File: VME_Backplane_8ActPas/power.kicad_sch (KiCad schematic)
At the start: 7 parts, among them U1 TCA0372, U2 TCA0372, X1 Conn_01x05

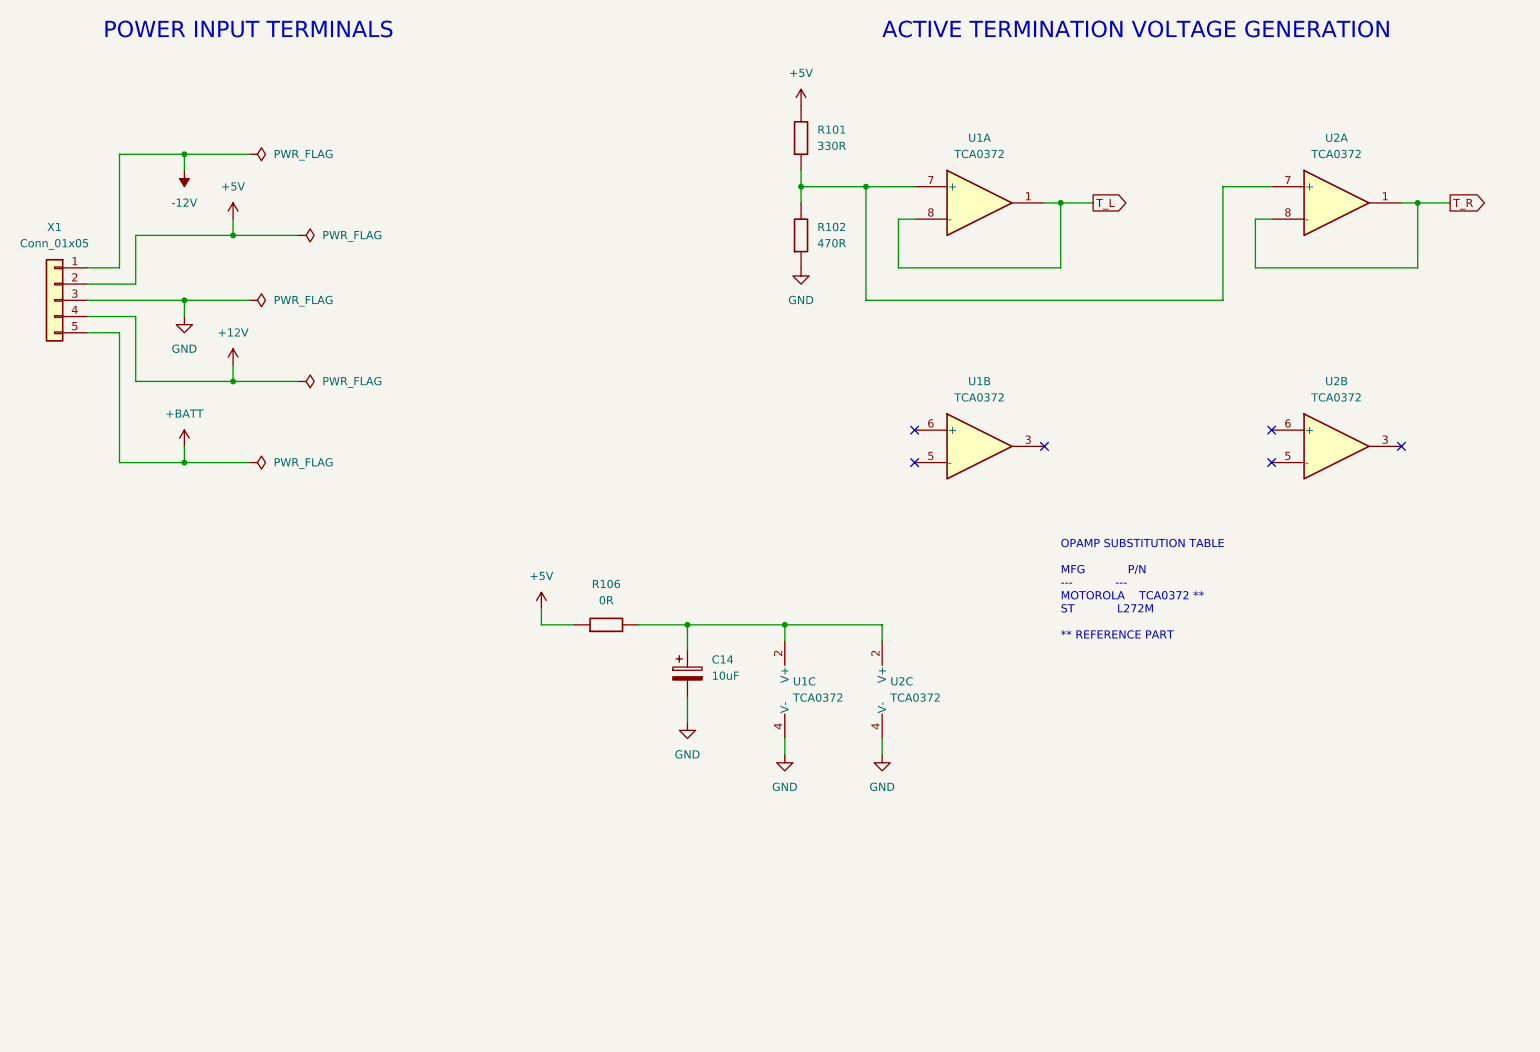
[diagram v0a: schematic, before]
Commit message: Give each opamp their own resistor divider due to separation
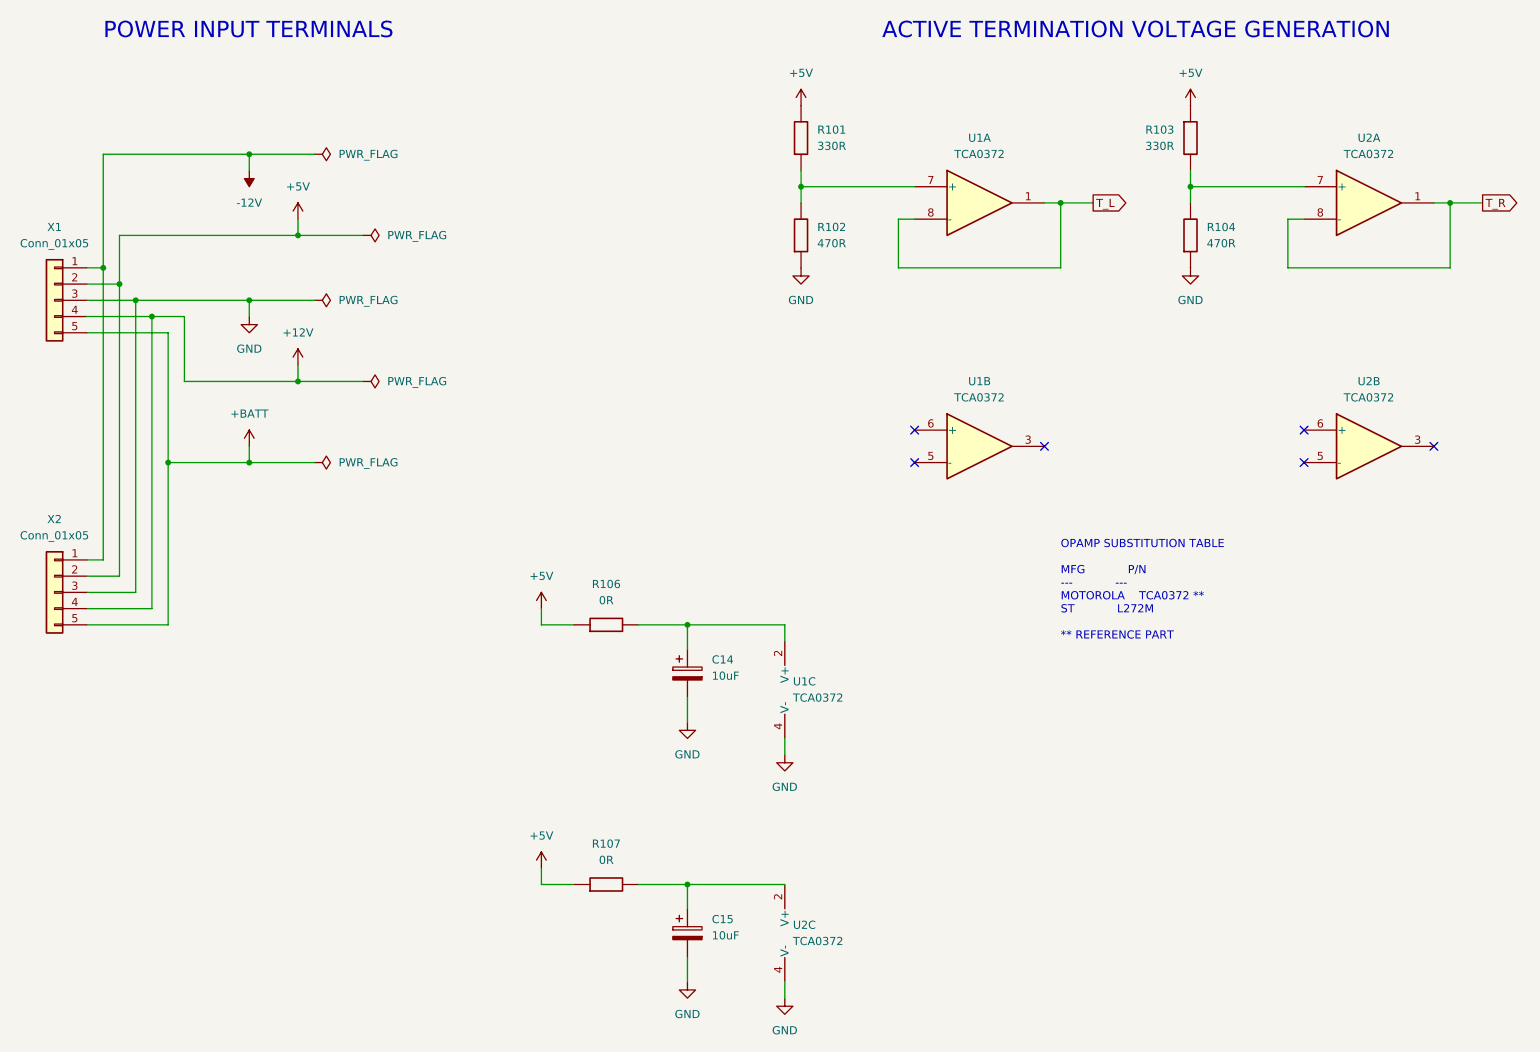
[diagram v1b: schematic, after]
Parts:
- added C15: 10uF, Capacitor_THT:CP_Radial_Tantal_D5.0mm_P5.00mm, symbol Device:C_Polarized
- added R103: 330R, Resistor_THT:R_Axial_DIN0207_L6.3mm_D2.5mm_P10.16mm_Horizontal, symbol COMET symbols:R
- added R104: 470R, Resistor_THT:R_Axial_DIN0207_L6.3mm_D2.5mm_P10.16mm_Horizontal, symbol COMET symbols:R
- added R107: 0R, Resistor_THT:R_Axial_DIN0207_L6.3mm_D2.5mm_P10.16mm_Horizontal, symbol COMET symbols:R
- added X2: Conn_01x05, TerminalBlock_Phoenix:TerminalBlock_Phoenix_MKDS-1,5-5-5.08_1x05_P5.08mm_Horizontal, symbol Connector_Generic:Conn_01x05
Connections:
- net +12V: now also X2.4 (Pin_4)
- net +5V: now also R103.2, R107.2, X2.2 (Pin_2)
- net +BATT: now also X2.5 (Pin_5)
- net -12V: now also X2.1 (Pin_1)
- net GND: now also C15.2, R104.2, X2.3 (Pin_3)
- net at C14.1, R106.1, U1.2 (V+): no longer U2.2 (V+)
- net at R101.2, R102.1, U1.7 (+): no longer U2.7 (+)
- new net: R103.1, R104.1, U2.7 (+)
- new net: C15.1, R107.1, U2.2 (V+)
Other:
- moved on the sheet: U2A, U2B, U2C

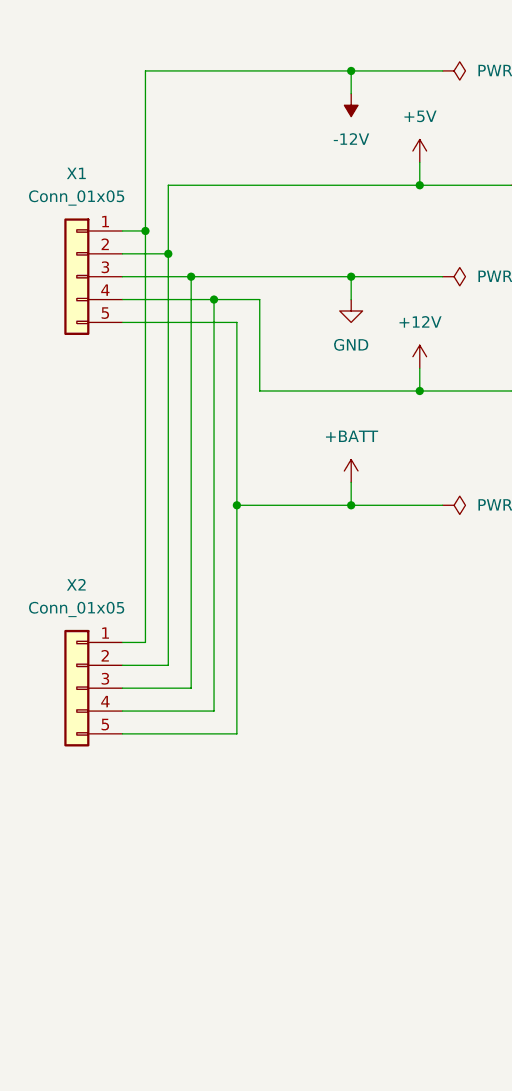
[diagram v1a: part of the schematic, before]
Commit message: Add second power inlet and +5V sense terminal block
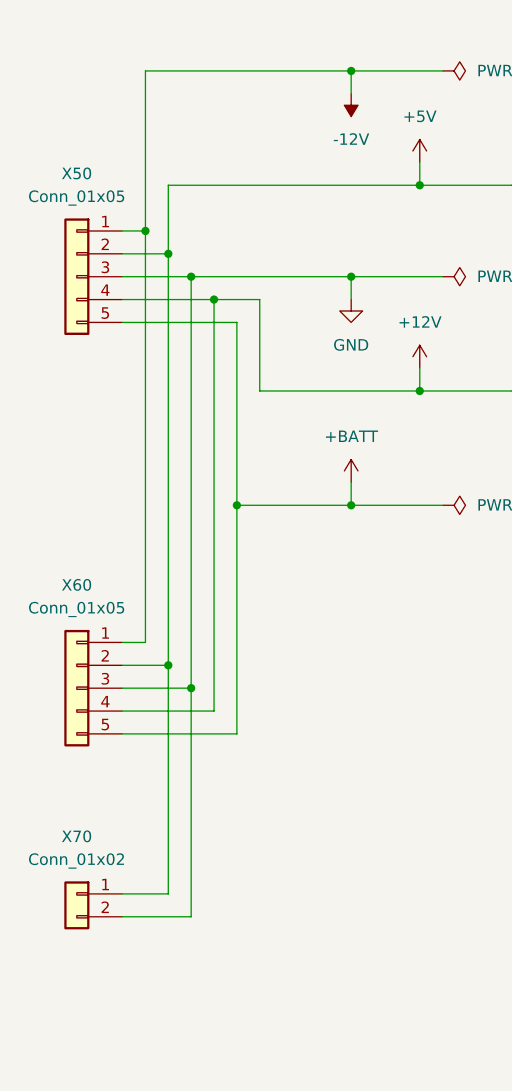
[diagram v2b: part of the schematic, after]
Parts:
- added X70: Conn_01x02, TerminalBlock_Phoenix:TerminalBlock_Phoenix_MKDS-1,5-2-5.08_1x02_P5.08mm_Horizontal, symbol Connector_Generic:Conn_01x02
- renumbered X1 to X50, X2 to X60
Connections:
- net +5V: now also X70.1 (Pin_1)
- net GND: now also X70.2 (Pin_2)
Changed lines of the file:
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@@
   (title_block
     (title "POWER INPUT AND TERMINATION VOLTAGES")
-    (date "2024-01-03")
+    (date "2024-01-04")
     (rev "1")
     (company "TOM STOREY")
@@
   (junction (at 38.1 73.66) (diameter 0) (color 0 0 0 0)
   )
+  (junction (at 40.64 121.92) (diameter 0) (color 0 0 0 0)
+  )
   (junction (at 58.42 101.6) (diameter 0) (color 0 0 0 0)
+  )
+  (junction (at 38.1 119.38) (diameter 0) (color 0 0 0 0)
   )
   (junction (at 40.64 76.2) (diameter 0) (color 0 0 0 0)
@@
     (stroke (width 0) (type default) (color 0 0 0 0))
   )
+  (wire (pts (xy 40.64 121.92) (xy 40.64 147.32))
+    (stroke (width 0) (type default) (color 0 0 0 0))
+  )
+  (wire (pts (xy 38.1 119.38) (xy 38.1 144.78))
+    (stroke (width 0) (type default) (color 0 0 0 0))
+  )
   (wire (pts (xy 127 179.07) (xy 127 182.88))
     (stroke (width 0) (type default) (color 0 0 0 0))
@@
     (stroke (width 0) (type default) (color 0 0 0 0))
   )
+  (wire (pts (xy 38.1 144.78) (xy 33.02 144.78))
+    (stroke (width 0) (type default) (color 0 0 0 0))
+  )
   (wire (pts (xy 109.22 127) (xy 104.14 127))
     (stroke (width 0) (type default) (color 0 0 0 0))
@@
   )
   (wire (pts (xy 127 127) (xy 142.24 127))
+    (stroke (width 0) (type default) (color 0 0 0 0))
+  )
+  (wire (pts (xy 40.64 147.32) (xy 33.02 147.32))
     (stroke (width 0) (type default) (color 0 0 0 0))
   )
@@
   (symbol (lib_id "Connector_Generic:Conn_01x05") (at 27.94 121.92 0) (mirror y) (unit 1)
     (in_bom yes) (on_board yes) (fields_autoplaced)
-    (property "Reference" "X2" (id 0) (at 27.94 110.49 0))
+    (property "Reference" "X60" (id 0) (at 27.94 110.49 0))
     (property "Value" "Conn_01x05" (id 1) (at 27.94 113.03 0))
     (property "Footprint" "TerminalBlock_Phoenix:TerminalBlock_Phoenix_MKDS-1,5-5-5.08_1x05_P5.08mm_Horizontal" (id 2) (at 27.94 121.92 0)
@@
   (symbol (lib_id "Connector_Generic:Conn_01x05") (at 27.94 76.2 0) (mirror y) (unit 1)
     (in_bom yes) (on_board yes) (fields_autoplaced)
-    (property "Reference" "X1" (id 0) (at 27.94 64.77 0))
+    (property "Reference" "X50" (id 0) (at 27.94 64.77 0))
     (property "Value" "Conn_01x05" (id 1) (at 27.94 67.31 0))
     (property "Footprint" "TerminalBlock_Phoenix:TerminalBlock_Phoenix_MKDS-1,5-5-5.08_1x05_P5.08mm_Horizontal" (id 2) (at 27.94 76.2 0)
@@
     (pin "1")
   )
+  (symbol (lib_id "Connector_Generic:Conn_01x02") (at 27.94 144.78 0) (mirror y) (unit 1)
+    (in_bom yes) (on_board yes) (fields_autoplaced)
+    (property "Reference" "X70" (id 0) (at 27.94 138.43 0))
+    (property "Value" "Conn_01x02" (id 1) (at 27.94 140.97 0))
+    (property "Footprint" "TerminalBlock_Phoenix:TerminalBlock_Phoenix_MKDS-1,5-2-5.08_1x02_P5.08mm_Horizontal" (id 2) (at 27.94 144.78 0)
+      (effects (font (size 1.27 1.27)) hide)
+    )
+    (property "Datasheet" "~" (id 3) (at 27.94 144.78 0)
+      (effects (font (size 1.27 1.27)) hide)
+    )
+    (pin "1")
+    (pin "2")
+  )
   (symbol (lib_id "COMET symbols:R") (at 144.78 50.8 0) (unit 1)

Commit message: Update resistor footprints with preferred silkscreen outlines
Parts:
- R101, R102, R103, R104, R106, R107: footprint Resistor_THT:R_Axial_DIN0207_L6.3mm_D2.5mm_P10.16mm_Horizontal -> COMET footprints:R_Axial_DIN0207_L6.3mm_D2.5mm_P10.16mm_Horizontal
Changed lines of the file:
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@@
     (property "Reference" "R106" (id 0) (at 114.3 120.65 90))
     (property "Value" "0R" (id 1) (at 114.3 123.19 90))
-    (property "Footprint" "Resistor_THT:R_Axial_DIN0207_L6.3mm_D2.5mm_P10.16mm_Horizontal" (id 2) (at 114.3 127 0)
+    (property "Footprint" "COMET footprints:R_Axial_DIN0207_L6.3mm_D2.5mm_P10.16mm_Horizontal" (id 2) (at 114.3 127 0)
       (effects (font (size 1.27 1.27)) hide)
     )
@@
       (effects (font (size 1.27 1.27)) (justify left))
     )
-    (property "Footprint" "Resistor_THT:R_Axial_DIN0207_L6.3mm_D2.5mm_P10.16mm_Horizontal" (id 2) (at 144.78 66.04 0)
+    (property "Footprint" "COMET footprints:R_Axial_DIN0207_L6.3mm_D2.5mm_P10.16mm_Horizontal" (id 2) (at 144.78 66.04 0)
       (effects (font (size 1.27 1.27)) hide)
     )
@@
     (property "Reference" "R107" (id 0) (at 114.3 161.29 90))
     (property "Value" "0R" (id 1) (at 114.3 163.83 90))
-    (property "Footprint" "Resistor_THT:R_Axial_DIN0207_L6.3mm_D2.5mm_P10.16mm_Horizontal" (id 2) (at 114.3 167.64 0)
+    (property "Footprint" "COMET footprints:R_Axial_DIN0207_L6.3mm_D2.5mm_P10.16mm_Horizontal" (id 2) (at 114.3 167.64 0)
       (effects (font (size 1.27 1.27)) hide)
     )
@@
       (effects (font (size 1.27 1.27)) (justify left))
     )
-    (property "Footprint" "Resistor_THT:R_Axial_DIN0207_L6.3mm_D2.5mm_P10.16mm_Horizontal" (id 2) (at 205.74 66.04 0)
+    (property "Footprint" "COMET footprints:R_Axial_DIN0207_L6.3mm_D2.5mm_P10.16mm_Horizontal" (id 2) (at 205.74 66.04 0)
       (effects (font (size 1.27 1.27)) hide)
     )
@@
       (effects (font (size 1.27 1.27)) (justify left))
     )
-    (property "Footprint" "Resistor_THT:R_Axial_DIN0207_L6.3mm_D2.5mm_P10.16mm_Horizontal" (id 2) (at 144.78 50.8 0)
+    (property "Footprint" "COMET footprints:R_Axial_DIN0207_L6.3mm_D2.5mm_P10.16mm_Horizontal" (id 2) (at 144.78 50.8 0)
       (effects (font (size 1.27 1.27)) hide)
     )
@@
       (effects (font (size 1.27 1.27)) (justify right))
     )
-    (property "Footprint" "Resistor_THT:R_Axial_DIN0207_L6.3mm_D2.5mm_P10.16mm_Horizontal" (id 2) (at 205.74 50.8 0)
-      (effects (font (size 1.27 1.27)) hide)
-    )
+    (property "Footprint" "COMET footprints:R_Axial_DIN0207_L6.3mm_D2.5mm_P10.16mm_Horizontal" (id 2) (at 205.74 50.8 0)
+      (effects (font (size 1.27 1.27)) hide)
+    )
